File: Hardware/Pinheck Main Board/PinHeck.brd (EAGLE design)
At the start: 359.2 x 152.3 mm, 363 parts, among them IC2 PIC32MX795F512L-80I/PT, IC3 CD74HCT244E, IC4 CD74HCT244E, IC5 ULN2803A, J3 N/A, J4 SJ1-2503A, P1 TC33X-2-103E, U1 P8X32A-Q44, U10 74HCT2G04GV,125, U11 CD74HC165M96, U12 CD74HC165M96, U13 CAT24M01LI-G, U14 MC74HC08ADR2G, U15 MC74HC08ADR2G, U16 MC74HC08ADR2G, U17 MC74HC08ADR2G, U18 MC74HC08ADR2G, U19 MC74HC08ADR2G, U2 DS1340Z-33+, U20 TIP107, U21 TIP107, U22 TIP107, U23 TIP107, U24 TIP107, U25 TIP107, U26 TIP107, U27 TIP107, U28 TIP102, U29 TIP102, U3 CD74HC595M96, U30 TIP102, U31 TIP102, U32 TIP102, U33 TIP102, U34 TIP102, U35 TIP102, U36 WS2801, U37 TIP102, U38 WS2801, U39 NCP1117DT33G, U4 CAT24M01LI-G, U40 TIP102, U41 TIP102, U42 TIP102, U43 TIP102, U44 TIP102, U45 TIP102, U46 TIP102, U47 TIP102, U48 TIP102, U49 TIP102, U5 CD74HC595M96, U50 TIP102, U51 TIP102, U52 CD74HC123M96, U6 TIP102, U7 TIP102, U8 TIP102, U9 TIP102, X1 FQ7050B-8.000, X2 9C-6.500MAAJ-T, X3 ABS25-32.768KHz-1-T

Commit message: Added changes for Ben
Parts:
- U37: value TIP102 -> TIP107
- moved U37 24.5 mm to (308.9, 114.3), turned to 180 degrees
- moved PIC_PROGRAM 17.8 mm to (116.1, 99.3)
- moved PROP_RST 14.5 mm to (219.5, 109.7)
- moved PROP_PROGRAM 14.1 mm to (204.7, 109.7)
- moved PIC_RST 11.7 mm to (134.1, 99.3)
- moved U$1 1.52 mm to (240.0, 93.0)
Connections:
- net AC_17 renamed SERVO_2
- net AC_33 renamed SERVO_4
- net AC_34 renamed SERVO_3
- net AC_44 renamed SERVO_1
- net AC_46 renamed SERVO_0
- net COMM_ATN renamed COMM_IN_TX
- net COMM_CLK renamed COMM_CLK_RX
- net COMM_DATA renamed COMM_OUT
- net DATA_CAB renamed CAB_SWITCH_IN
- net DATA_CLK renamed CAB_CLK
- net DATA_LAT renamed CAB_LAT
- net GI_DATA_COL renamed CAB_GI_OUT
- net MENU renamed BACK
- net RG9 renamed PIC_PROGRAM_SW
- removed net RC1: IC2.6
- removed net RG6: IC2.10
- new net EXT_RGB_CLK: IC2.6, RGB_COM_OUT.P$3
- new net EXT_RGB_DATA: IC2.10, RGB_COM_OUT.P$2
- net 5V: now also R115.1, U37.S
- net GND: no longer R115.1, U37.S
- net RGB_CLK_OUT: no longer RGB_COM_OUT.P$3
- net RGB_DATA_OUT: no longer RGB_COM_OUT.P$2
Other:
- board text removed: "Andrew Edgerton"

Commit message: Routing external connectors first. Working my way inwards.
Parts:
- removed J6: (no value), PP_Connectors:26-64-4110(KEYPIN3)
- added CAB_RGB: (no value), PP_Connectors:26-64-4110(KEYPIN3)
- moved LOGO1 97.9 mm to (-55.1, 68.1)
- moved R75 62.9 mm to (47.0, 71.6)
- moved R76 61.9 mm to (49.8, 71.6)
- moved R77 57.6 mm to (52.3, 71.6)
- moved R78 56.7 mm to (55.1, 71.6)
- moved R82 55.7 mm to (69.6, 71.6)
- moved R79 55.7 mm to (57.7, 71.6)
- moved R80 54.5 mm to (60.2, 71.6)
- moved R81 54.0 mm to (63.2, 71.6)
- moved R34 46.3 mm to (298.2, 153.4), turned to 90 degrees
- moved R32 44.9 mm to (292.9, 153.4), turned to 90 degrees
- moved IC3 38.9 mm to (59.4, 82.0)
- moved SOCKET1 38.9 mm to (59.4, 82.0)
- moved R116 22.9 mm to (304.8, 115.3), turned to 180 degrees
- moved R115 21.2 mm to (304.8, 112.8), turned to 0 degrees
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- renumbered J4 to AUDIO
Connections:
- net 12V: now also CAB_RGB.P$1, CAB_RGB.P$2; no longer J6.P$1, J6.P$2
- net GND: now also CAB_RGB.P$10, CAB_RGB.P$9; no longer J6.P$10, J6.P$9
- net RGB_BOUT_L: now also CAB_RGB.P$3; no longer J6.P$3
- net RGB_BOUT_R: now also CAB_RGB.P$6; no longer J6.P$6
- net RGB_GOUT_L: now also CAB_RGB.P$4; no longer J6.P$4
- net RGB_GOUT_R: now also CAB_RGB.P$7; no longer J6.P$7
- net RGB_ROUT_L: now also CAB_RGB.P$5; no longer J6.P$5
- net RGB_ROUT_R: now also CAB_RGB.P$8; no longer J6.P$8
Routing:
- net 12V: track 0.00 -> 152.4 mm, vias 0 -> 8
- net GND: track 6.95 -> 133.9 mm, vias 2 -> 70
- net SW_R_6: track 0.00 -> 94.1 mm
- net SW_R_4: track 0.00 -> 87.4 mm
- net SW_R_7: track 0.00 -> 87.1 mm
- net SW_R_2: track 0.00 -> 84.9 mm
- net SW_R_0: track 0.00 -> 84.2 mm
- net SW_R_5: track 0.00 -> 80.2 mm
- net SW_R_3: track 0.00 -> 77.6 mm
- net SW_R_1: track 0.00 -> 74.9 mm
- net 3.3V: track 0.00 -> 68.2 mm, vias 0 -> 71
- net 5V: track 18.2 -> 83.6 mm, vias 6 -> 22
- net N$14: track 0.00 -> 44.0 mm
- net N$6: track 0.00 -> 42.0 mm
- net N$11: track 0.00 -> 42.0 mm
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- added copper zone on layer 1, net 3.3V
- added copper zone on layer 1, net GND
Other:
- board text removed: "12V"
- board text removed: "AUDIO"
- board text removed: "EEPROM"
- board text removed: "R_0"
- board text removed: "R_1"
- board text removed: "R_2"
- board text removed: "R_3"
- board text removed: "R_4"
- board text removed: "R_5"
- board text removed: "R_6"
- board text removed: "R_7"

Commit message: have all the peripherals layed out on the new pinheck
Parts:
- removed J3: N/A, PP_Connectors:2.54MM_01X04_PIN_HEADER
- removed U40, U41, U42, U43, U44, U45, U46, U47, U48, U49, U50, U51, U6, U7, U8, U9: TIP102, PP_DiscreteSemi:TO-220AB
- added C29: MF-CAP-12.5MM-1000uF, MF_Passives:CP6.3MM
- added C30: .1uF, PP_Passives:0805
- added F5: 4245K, PP_Passives:4245K
- added GI0, GI1, GI10, GI11, GI12, GI13, GI14, GI15, GI2, GI3, GI4, GI5, GI6, GI7, GI8, GI9: TIP102, PP_DiscreteSemi:TO-220AB
- moved PROP_UART 96.8 mm to (117.6, 188.7), turned to 180 degrees
- moved PICKIT3 91.2 mm to (100.8, 188.7), turned to 180 degrees
- moved PICKIT3_TC 91.1 mm to (100.8, 181.9), turned to 180 degrees
- moved PROP_TC 87.7 mm to (117.6, 181.9), turned to 180 degrees
- moved PIC32_UART 73.0 mm to (84.1, 188.7), turned to 180 degrees
- moved PIC32_TC 66.1 mm to (84.1, 181.9), turned to 180 degrees
- moved U10 25.2 mm to (296.2, 125.7), turned to 270 degrees
- moved C26 16.5 mm to (288.8, 102.6)
- moved R125 16.5 mm to (285.8, 94.7)
- moved R126 16.5 mm to (288.3, 94.7)
- moved R127 16.5 mm to (290.8, 94.7)
- moved R128 16.5 mm to (293.4, 94.7)
- moved R129 16.5 mm to (295.9, 94.7)
- moved R130 16.5 mm to (298.4, 94.7)
- moved R131 16.5 mm to (301.0, 94.7)
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- renumbered J7 to DMD_PWR
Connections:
- removed net GI_5V: F4.2A, F4.2B, GI_0.P$10, GI_1.P$9
- removed net GI_R_15: GI_1.P$8, U51.D
- new net GI0_5V: F5.2A, F5.2B, GI_0.P$10
- new net GI15: GI15.D, GI_1.P$8
- new net GI1_5V: F4.2A, F4.2B, GI_1.P$9
- net !AN_BLANK: no longer J3.4
- net 12V: now also C29.P$1
- net 5V: now also C30.1, F5.1A, F5.1B
- net GI_R_0: now also GI0.D; no longer U6.D
- net GI_R_1: now also GI1.D; no longer U7.D
- net GI_R_10: now also GI10.D; no longer U46.D
- net GI_R_11: now also GI11.D; no longer U47.D
- net GI_R_12: now also GI12.D; no longer U48.D
- net GI_R_13: now also GI13.D; no longer U49.D
- net GI_R_14: now also GI14.D; no longer U50.D
- net GI_R_2: now also GI2.D; no longer U8.D
- net GI_R_3: now also GI3.D; no longer U9.D
- net GI_R_4: now also GI4.D; no longer U40.D
- net GI_R_5: now also GI5.D; no longer U41.D
- net GI_R_6: now also GI6.D; no longer U42.D
- net GI_R_7: now also GI7.D; no longer U43.D
- net GI_R_8: now also GI8.D; no longer U44.D
- net GI_R_9: now also GI9.D; no longer U45.D
- net GND: now also C29.P$2, C30.2, GI0.S, GI1.S, GI10.S, GI11.S, GI12.S, GI13.S, GI14.S, GI15.S, GI2.S, GI3.S, GI4.S, GI5.S, GI6.S, GI7.S, GI8.S, GI9.S; no longer J3.2, J3.3, U40.S, U41.S, U42.S, U43.S, U44.S, U45.S, U46.S, U47.S, U48.S, U49.S, U50.S, U51.S, U6.S, U7.S, U8.S, U9.S
- net N$481: now also GI0.G; no longer U6.G
- net N$482: now also GI1.G; no longer U7.G
- net N$483: now also GI2.G; no longer U8.G
- net N$484: now also GI3.G; no longer U9.G
- net N$485: now also GI4.G; no longer U40.G
- net N$486: now also GI5.G; no longer U41.G
- net N$487: now also GI6.G; no longer U42.G
- net N$488: now also GI7.G; no longer U43.G
- net N$489: now also GI8.G; no longer U44.G
- net N$490: now also GI9.G; no longer U45.G
- net N$491: now also GI10.G; no longer U46.G
- net N$492: now also GI11.G; no longer U47.G
- net N$493: now also GI12.G; no longer U48.G
- net N$494: now also GI13.G; no longer U49.G
- net N$495: now also GI14.G; no longer U50.G
- net N$496: now also GI15.G; no longer U51.G
- net WATCHDOG: no longer J3.1
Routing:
- net WATCHDOG: track 0.00 -> 245.6 mm, vias 0 -> 24
- net GND: track 133.9 -> 250.8 mm, vias 70 -> 112
- net 5V: track 83.6 -> 168.1 mm, vias 22 -> 28
- net CAB_CLK: track 0.00 -> 80.1 mm
- net GI15: track 0.00 -> 78.8 mm
- net GI_R_14: track 0.00 -> 68.5 mm
- net GI1_5V: track 0.00 -> 62.4 mm
- net N$481: track 0.00 -> 60.6 mm
- net GI_R_13: track 0.00 -> 58.2 mm
- net N$489: track 0.00 -> 56.4 mm
- net N$482: track 0.00 -> 51.7 mm
- net N$490: track 0.00 -> 51.3 mm
- net !DATA_LAT: track 0.00 -> 48.9 mm
- net GI_R_12: track 0.00 -> 48.3 mm
- net N$491: track 0.00 -> 46.5 mm
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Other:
- board text removed: "5V"
- board text removed: "AN_"
- board text removed: "GND"
- board text removed: "WD"

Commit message: Prop routed. Pic32 started.
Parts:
- added C31, C47, C54, C55: .1uF, PP_Passives:0805
- added C49: EEE-1VA101XP, PP_Passives:6.3MM_CAP_SMD
- moved U$1 287.8 mm to (-36.1, 174.2)
- moved U$2 242.8 mm to (-36.3, 199.9)
- moved C1 97.1 mm to (137.4, 181.9)
- moved C21 93.8 mm to (184.7, 124.7), turned to 270 degrees
- moved C20 84.0 mm to (177.3, 114.4)
- moved R176 79.0 mm to (201.2, 103.6), turned to 90 degrees
- moved C23 69.3 mm to (196.1, 115.2)
- moved C22 63.9 mm to (188.0, 124.7), turned to 90 degrees
- moved R30 63.2 mm to (177.8, 127.5), turned to 270 degrees
- moved PROP_ACT 62.5 mm to (177.8, 122.9), turned to 270 degrees
- moved C28 61.0 mm to (179.3, 147.3)
- moved SOCKET5 61.0 mm to (185.9, 147.3)
- moved U13 61.0 mm to (185.9, 147.3)
- moved R24 61.0 mm to (187.2, 154.8)
- moved R25 61.0 mm to (189.7, 154.8)
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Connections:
- net N$24 renamed SD_IQ
- net P0 renamed SD_DO
- net P1 renamed SD_SCLK
- net P13 renamed PROP_PROGRAM
- net P2 renamed SD_DI
- net P27 renamed PROP_ACT
- net P3 renamed SD_CS
- removed net P14: R32.1, U1.15
- removed net P15: R34.1, U1.16
- removed net P16: DMD_CON.11, U1.19
- removed net P17: DMD_CON.9, U1.20
- removed net P18: DMD_CON.7, U1.21
- removed net P19: DMD_CON.5, U1.22
- removed net P20: DMD_CON.3, U1.23
- removed net P21: DMD_CON.1, U1.24
- removed net P22: U1.25
- new net AUD0: R32.1, U1.16
- new net AUD1: R34.1, U1.15
- new net DMD_1: DMD_CON.1, U1.25
- new net DMD_11: DMD_CON.11, U1.20
- new net DMD_13: DMD_CON.13, U1.19
- new net DMD_3: DMD_CON.3, U1.24
- new net DMD_5: DMD_CON.5, U1.23
- new net DMD_7: DMD_CON.7, U1.22
- new net DMD_9: DMD_CON.9, U1.21
- net 3.3V: now also C31.2, C47.2, C49.POS, C54.2, C55.2
- net GND: now also C31.1, C47.1, C49.NEG, C54.1, C55.1
- net P8: no longer DMD_CON.13
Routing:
- net PIC_SW_C_7: track 0.00 -> 133.3 mm, vias 0 -> 1
- net AUD1: track 0.00 -> 132.0 mm
- net AUD0: track 0.00 -> 131.1 mm
- net PIC_SW_C_4: track 0.00 -> 126.4 mm, vias 0 -> 1
- net SD_DO: track 3.24 -> 128.9 mm, vias 0 -> 2
- net PIC_SW_C_6: track 0.00 -> 124.5 mm, vias 0 -> 1
- net PIC_SW_C_5: track 0.00 -> 124.4 mm, vias 0 -> 1
- net SD_SCLK: track 3.19 -> 127.2 mm, vias 0 -> 2
- net PIC_SOL_3: track 9.56 -> 132.3 mm, vias 0 -> 2
- net PIC_SW_C_2: track 0.00 -> 117.7 mm, vias 0 -> 1
- net SD_DI: track 3.19 -> 120.8 mm, vias 0 -> 2
- net SD_CS: track 3.17 -> 119.3 mm, vias 0 -> 2
- net PIC_SW_C_3: track 0.00 -> 112.6 mm, vias 0 -> 1
- net 3.3V: track 78.8 -> 185.1 mm, vias 72 -> 96
- net GND: track 250.8 -> 354.0 mm, vias 112 -> 130
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
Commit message: Home stretch!
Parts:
- removed D8: NSQA6V8AW5T2G, Discrete:SOT-323-5
- MOD_CON: device PP_Connectors:2.54MM_01X05_PIN_HEADER -> PP_Connectors:2.54MM_01X06_PIN_HEADER
- moved PROP_UART 150.0 mm to (86.4, 42.0), turned to 90 degrees
- moved PROP_TC 142.5 mm to (79.5, 44.6), turned to 90 degrees
- moved LOGO1 133.2 mm to (74.7, 97.8)
- moved PIC32_UART 128.4 mm to (86.4, 60.3), turned to 90 degrees
- moved PIC32_TC 119.1 mm to (79.5, 62.9), turned to 90 degrees
- moved C1 105.6 mm to (195.6, 93.7), turned to 180 degrees
- moved PICKIT3 105.4 mm to (86.4, 84.3), turned to 90 degrees
- moved PICKIT3_TC 103.3 mm to (79.5, 80.8), turned to 90 degrees
- moved R26 83.6 mm to (86.4, 72.1)
- moved R14 79.5 mm to (79.8, 99.3)
- moved R13 74.9 mm to (82.5, 99.3), turned to 270 degrees
- moved R137 62.8 mm to (93.2, 93.2), turned to 270 degrees
- moved R4 46.3 mm to (113.0, 95.2), turned to 90 degrees
- moved D1 38.6 mm to (119.6, 99.8), turned to 270 degrees
- moved R12 33.6 mm to (126.0, 95.2), turned to 270 degrees
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- renumbered U37 to ST_LI
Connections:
- removed net !AN_BLANK: U10.4
- net 12V: now also MOD_CON.6
- net AUX_3: now also R15.1; no longer R5.1
- net AUX_4: now also R10.1; no longer R7.1
- net AUX_5: now also R7.1; no longer R10.1
- net AUX_6: now also R5.1; no longer R15.1
- net GND: no longer D8.2
- net N$31: no longer D8.4
- net N$33: no longer D8.5
- net P32_MCLR: no longer D8.3
- net WATCHDOG: no longer U10.3
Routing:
- net 12V: track 165.0 -> 574.5 mm, vias 8 -> 13
- net AUX_6: track 1.50 -> 291.9 mm, vias 0 -> 2
- net AUX_5: track 1.50 -> 287.7 mm, vias 0 -> 2
- net AUX_4: track 1.50 -> 281.0 mm, vias 0 -> 2
- net AUX_3: track 1.50 -> 274.3 mm, vias 0 -> 2
- net AUX_0: track 1.50 -> 252.6 mm, vias 0 -> 2
- net AUX_1: track 1.50 -> 250.1 mm, vias 0 -> 2
- net AUX_2: track 1.50 -> 247.5 mm, vias 0 -> 2
- net PIC_LIGHT_C_7: track 0.00 -> 239.9 mm, vias 0 -> 3
- net ST_LI_GATE: track 0.00 -> 233.3 mm, vias 0 -> 2
- net PIC_LIGHT_C_6: track 0.00 -> 229.0 mm, vias 0 -> 3
- net CAB_SWITCH_IN: track 0.00 -> 227.3 mm, vias 0 -> 2
- net CAB_GI_OUT: track 0.00 -> 203.3 mm, vias 0 -> 2
- net CAB_LAT: track 34.7 -> 236.8 mm
- net CAB_CLK: track 80.1 -> 277.6 mm, vias 0 -> 4
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
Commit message: MOD CON area done. Starting test header.
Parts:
- moved U$1 144.2 mm to (98.3, 121.9)
- moved C46 2.29 mm to (272.0, 136.1)
- moved R18 2.29 mm to (268.5, 136.1)
- moved R19 2.29 mm to (275.8, 136.1)
- moved R22 2.29 mm to (265.9, 136.1)
- moved R23 2.29 mm to (263.4, 136.1)
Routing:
- net I2C_SCL: track 180.4 -> 233.3 mm
- net I2C_SDA: track 182.7 -> 231.1 mm
- net 12V: track 574.5 -> 597.1 mm
- net 3.3V: track 247.1 -> 256.2 mm
- net DMD_1: track 60.1 -> 63.1 mm
- net DMD_3: track 61.9 -> 64.8 mm
- net DMD_5: track 63.7 -> 66.5 mm
- net DMD_7: track 68.0 -> 70.8 mm
- net DMD_13: track 76.8 -> 79.6 mm
- net DMD_9: track 70.9 -> 73.6 mm
- net DMD_11: track 73.8 -> 76.5 mm
- net GND: track 387.9 -> 390.2 mm
- net N$19: track 3.17 -> 5.46 mm
- net CAB_SWITCH_IN: track 227.3 -> 225.3 mm
- net CAB_LAT: track 236.8 -> 238.7 mm
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
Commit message: First draft layout complete. Still need to wire in edge connector.
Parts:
- moved U$2 240.7 mm to (164.1, 66.5)
- moved AUDIO 29.8 mm to (315.5, 151.9)
- moved C53 29.8 mm to (338.2, 135.1)
- moved H33 29.8 mm to (354.6, 75.7)
- moved J12 29.8 mm to (265.7, 152.3)
- moved R46 29.8 mm to (341.1, 127.8)
- moved R50 29.8 mm to (341.1, 100.1)
- moved ST_LI 29.8 mm to (333.5, 91.9)
- moved C25 29.8 mm to (331.2, 80.8)
- moved C30 29.8 mm to (313.2, 103.6)
- moved C32 29.8 mm to (332.2, 125.7)
- moved C33 29.8 mm to (332.2, 108.0)
- moved C46 29.8 mm to (292.1, 114.0)
- moved F1 29.8 mm to (264.9, 44.2)
- moved F5 29.8 mm to (327.7, 44.2)
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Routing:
- net 3.3V: track 256.2 -> 243.4 mm

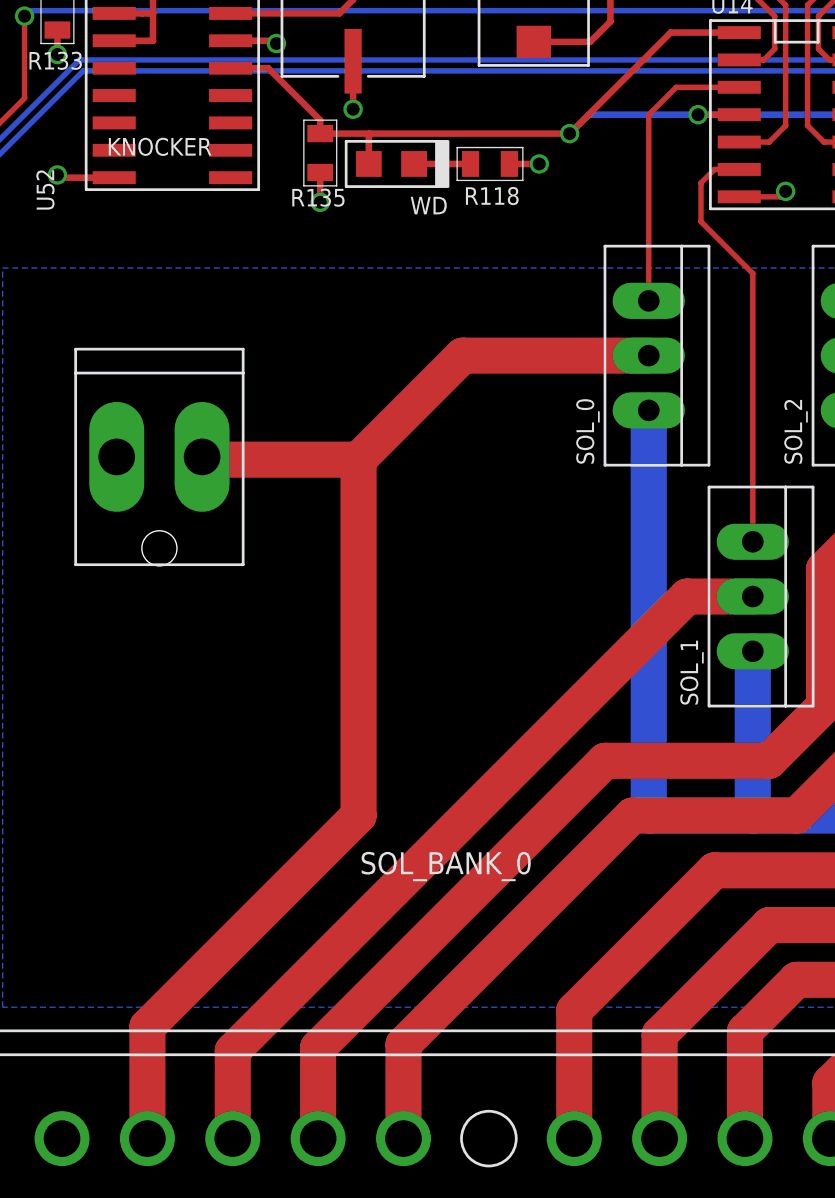
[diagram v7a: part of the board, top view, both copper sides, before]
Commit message: Added Shaker connector.
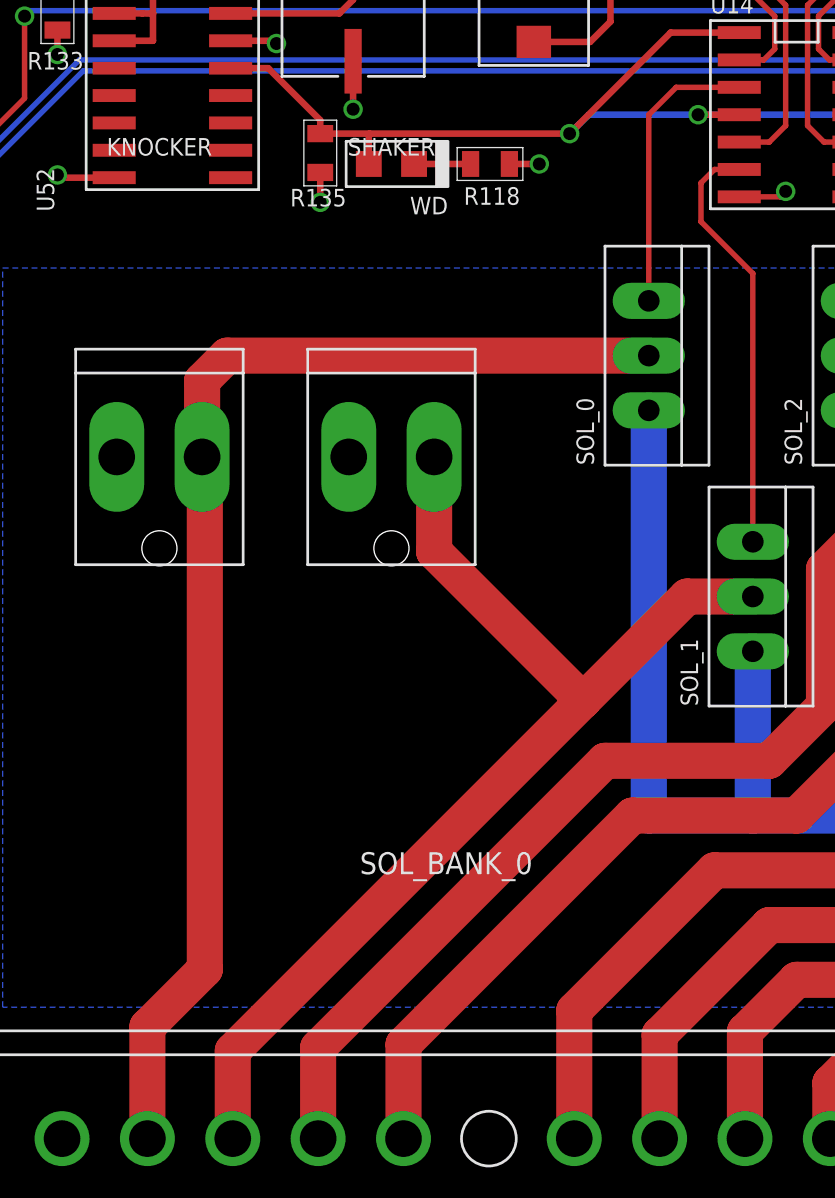
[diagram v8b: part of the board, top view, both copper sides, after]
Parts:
- added SHAKER: 26-64-4020, PP_Connectors:26-64-4020
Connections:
- net 50V_FUSE_0: now also SHAKER.P$1
- net SOL_PWR_1: now also SHAKER.P$2
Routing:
- net SOL_PWR_1: track 36.9 -> 51.1 mm
- net 50V_FUSE_0: track 188.6 -> 202.7 mm
- net SOL_PWR_0: track 58.3 -> 57.5 mm
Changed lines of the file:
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@@
 <element name="C54" library="PP_Passives" package="0805" value=".1uF" x="180.086" y="119.38"/>
 <element name="C55" library="PP_Passives" package="0805" value=".1uF" x="166.116" y="119.38"/>
+<element name="SHAKER" library="PP_Connectors" package="26-64-4020" value="26-64-4020" x="130.81" y="37.719">
+<attribute name="LABEL02" value="" x="122.682" y="58.293" size="1.778" layer="27" display="off"/>
+<attribute name="LABEL01" value="" x="122.682" y="58.293" size="1.778" layer="27" display="off"/>
+</element>
 </elements>
 <signals>
@@
 <wire x1="115.53" y1="13.676" x2="124.206" y2="22.352" width="3.81" layer="3"/>
 <wire x1="124.206" y1="22.352" x2="125.476" y2="23.622" width="3.81" layer="3"/>
-<wire x1="125.476" y1="23.622" x2="262.636" y2="23.622" width="3.81" layer="3"/>
+<wire x1="125.476" y1="23.622" x2="128.778" y2="23.622" width="3.81" layer="3"/>
+<wire x1="128.778" y1="23.622" x2="262.636" y2="23.622" width="3.81" layer="3"/>
 <wire x1="262.636" y1="23.622" x2="264.922" y2="25.908" width="3.81" layer="3"/>
 <wire x1="264.922" y1="25.908" x2="264.922" y2="26.731" width="3.81" layer="3"/>
@@
 <wire x1="117.856" y1="37.50825" x2="117.856" y2="28.702" width="1.6764" layer="3"/>
 <wire x1="117.856" y1="28.702" x2="124.206" y2="22.352" width="1.6764" layer="3"/>
+<contactref element="SHAKER" pad="P$1"/>
+<wire x1="128.83" y1="37.719" x2="128.83" y2="23.674" width="1.6764" layer="3"/>
+<wire x1="128.83" y1="23.674" x2="128.778" y2="23.622" width="1.6764" layer="3"/>
 </signal>
 <signal name="SOL_PWR_0">
@@
 <contactref element="SOL_BANK_0" pad="P$2"/>
 <contactref element="KNOCKER" pad="P$2"/>
-<wire x1="129.286" y1="37.592" x2="134.112" y2="42.418" width="1.6764" layer="1"/>
-<wire x1="134.112" y1="42.418" x2="142.748" y2="42.418" width="1.6764" layer="1"/>
 <wire x1="119.49" y1="6.096" x2="119.49" y2="11.286" width="1.6764" layer="1"/>
-<wire x1="119.49" y1="11.286" x2="129.286" y2="21.082" width="1.6764" layer="1"/>
-<wire x1="129.286" y1="21.082" x2="129.286" y2="37.592" width="1.6764" layer="1"/>
 <wire x1="122.02675" y1="37.719" x2="122.15375" y2="37.592" width="1.6764" layer="1"/>
-<wire x1="122.15375" y1="37.592" x2="129.286" y2="37.592" width="1.6764" layer="1"/>
+<wire x1="142.748" y1="42.418" x2="123.19" y2="42.418" width="1.6764" layer="1"/>
+<wire x1="123.19" y1="42.418" x2="122.02675" y2="41.25475" width="1.6764" layer="1"/>
+<wire x1="122.02675" y1="41.25475" x2="122.02675" y2="37.719" width="1.6764" layer="1"/>
+<wire x1="122.15375" y1="37.592" x2="122.15375" y2="13.94975" width="1.6764" layer="1"/>
+<wire x1="122.15375" y1="13.94975" x2="119.49" y2="11.286" width="1.6764" layer="1"/>
 </signal>
 <signal name="SOL_PWR_1">
@@
 <contactref element="SOL_BANK_0" pad="P$3"/>
 <wire x1="147.574" y1="31.242" x2="144.526" y2="31.242" width="1.6764" layer="1"/>
-<wire x1="144.526" y1="31.242" x2="123.45" y2="10.166" width="1.6764" layer="1"/>
+<wire x1="144.526" y1="31.242" x2="139.7" y2="26.416" width="1.6764" layer="1"/>
+<wire x1="139.7" y1="26.416" x2="123.45" y2="10.166" width="1.6764" layer="1"/>
 <wire x1="123.45" y1="10.166" x2="123.45" y2="6.096" width="1.6764" layer="1"/>
+<contactref element="SHAKER" pad="P$2"/>
+<wire x1="132.79" y1="37.719" x2="132.79" y2="33.326" width="1.6764" layer="1"/>
+<wire x1="132.79" y1="33.326" x2="139.7" y2="26.416" width="1.6764" layer="1"/>
 </signal>
 <signal name="SOL_PWR_2">
